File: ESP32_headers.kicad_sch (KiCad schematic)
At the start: 2 parts, among them J1 Conn_01x15_Socket, J2 Conn_01x15_Socket

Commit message: merge labels
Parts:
- removed J1, J2: Conn_01x15_Socket, Connector_PinSocket_2.54mm:PinSocket_1x15_P2.54mm_Vertical, symbol Connector:Conn_01x15_Socket
- added J8, J9: Conn_01x15_Socket, Connector_PinSocket_2.54mm:PinSocket_1x15_P2.54mm_Vertical, symbol Connector:Conn_01x15_Socket
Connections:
- new net +5V: J8.15 (Pin_15)
- new net 3.3V: J9.1 (Pin_1)
- new net D12: J8.12 (Pin_12)
- new net D13: J8.13 (Pin_13)
- new net D14: J8.11 (Pin_11)
- new net D15: J9.3 (Pin_3)
- new net D18: J9.9 (Pin_9)
- new net D19: J9.10 (Pin_10)
- new net D2: J9.4 (Pin_4)
- new net D21: J9.11 (Pin_11)
- new net D22: J9.14 (Pin_14)
- new net D23: J9.15 (Pin_15)
- new net D25: J8.8 (Pin_8)
- new net D26: J8.9 (Pin_9)
- new net D27: J8.10 (Pin_10)
- new net D32: J8.6 (Pin_6)
- new net D33: J8.7 (Pin_7)
- new net D34: J8.4 (Pin_4)
- new net D35: J8.5 (Pin_5)
- new net D4: J9.5 (Pin_5)
- new net D5: J9.8 (Pin_8)
- new net EN: J8.1 (Pin_1)
- new net GND: J8.14 (Pin_14), J9.2 (Pin_2)
- new net RX: J9.12 (Pin_12)
- new net RX2: J9.6 (Pin_6)
- new net TX: J9.13 (Pin_13)
- new net TX2: J9.7 (Pin_7)
- new net VN: J8.3 (Pin_3)
- new net VP: J8.2 (Pin_2)

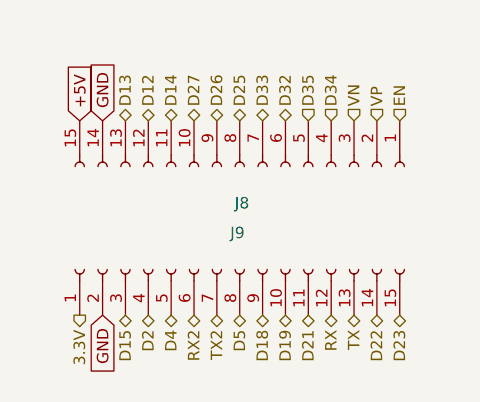
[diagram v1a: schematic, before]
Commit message: PCB Wiring to ESP32
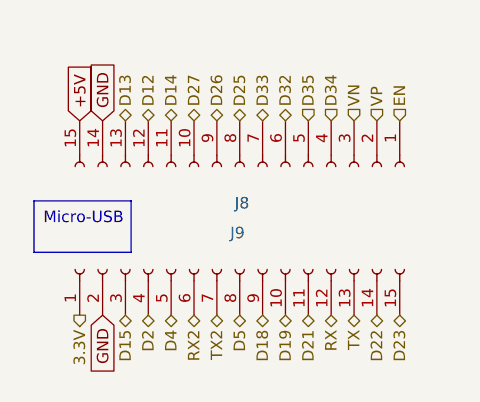
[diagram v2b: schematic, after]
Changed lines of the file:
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@@
 	(generator_version "8.0")
 	(paper "A4")
+	(text_box "Micro-USB"
+		(exclude_from_sim no)
+		(at 35.56 63.5 0)
+		(size 10.795 5.715)
+		(stroke
+			(width 0)
+			(type default)
+		)
+		(fill
+			(type none)
+		)
+		(effects
+			(font
+				(size 1.27 1.27)
+			)
+			(justify left top)
+		)
+	)
 	(global_label "GND"
 		(shape input)

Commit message: mounting holes
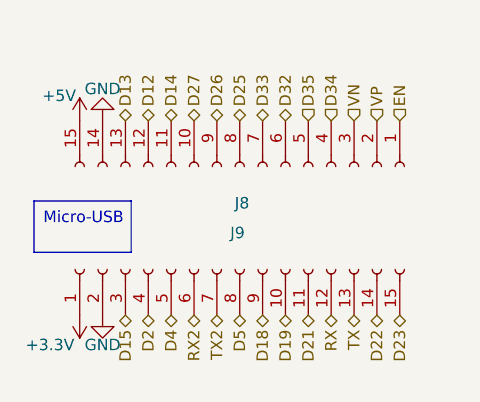
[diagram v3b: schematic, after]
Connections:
- net 3.3V renamed +3.3V

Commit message: adds test & test points
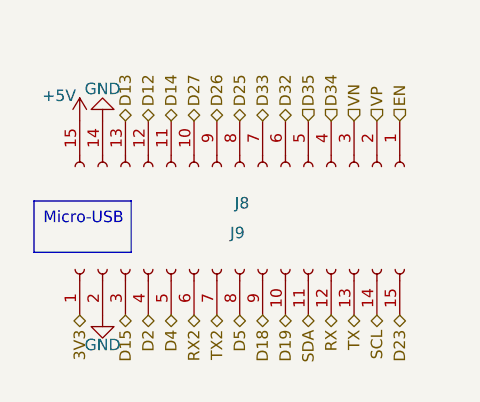
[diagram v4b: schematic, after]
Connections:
- net +3.3V renamed 3V3
- net D21 renamed SDA
- net D22 renamed SCL
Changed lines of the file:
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@@
 		)
 	)
-	(hierarchical_label "D21"
+	(hierarchical_label "SDA"
 		(shape bidirectional)
 		(at 66.04 76.2 270)
@@
 		)
 	)
-	(hierarchical_label "D22"
+	(hierarchical_label "SCL"
 		(shape bidirectional)
 		(at 73.66 76.2 270)
@@
 			)
 			(justify left)
+		)
+	)
+	(hierarchical_label "3V3"
+		(shape bidirectional)
+		(at 40.64 76.2 270)
+		(fields_autoplaced yes)
+		(effects
+			(font
+				(size 1.27 1.27)
+			)
+			(justify right)
 		)
 	)
@@
 					(unit 1)
 				)
-			)
-		)
-	)
-	(symbol
-		(lib_id "power:+3.3V")
-		(at 40.64 76.2 180)
-		(unit 1)
-		(exclude_from_sim no)
-		(in_bom yes)
-		(on_board yes)
-		(dnp no)
-		(property "Reference" "#PWR050"
-			(at 40.64 72.39 0)
-			(effects
-				(font
-					(size 1.27 1.27)
-				)
-				(hide yes)
-			)
-		)
-		(property "Value" "+3.3V"
-			(at 37.338 79.502 0)
-			(effects
-				(font
-					(size 1.27 1.27)
-				)
-			)
-		)
-		(property "Footprint" ""
-			(at 40.64 76.2 0)
-			(effects
-				(font
-					(size 1.27 1.27)
-				)
-				(hide yes)
-			)
-		)
-		(property "Datasheet" ""
-			(at 40.64 76.2 0)
-			(effects
-				(font
-					(size 1.27 1.27)
-				)
-				(hide yes)
-			)
-		)
-		(property "Description" "Power symbol creates a global label with name \"+3.3V\""
-			(at 40.64 76.2 0)
-			(effects
-				(font
-					(size 1.27 1.27)
-				)
-				(hide yes)
-			)
-		)
-		(pin "1"
-		)
-		(instances
-			(project "JAS Warhead PCB"
-				(path "/a037544f-9a20-478c-bac0-d162f9edf245/e02061e8-dea8-4b91-abef-2bf744ccc8cc"
-					(reference "#PWR050")
-					(unit 1)
-				)

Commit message: start compliance with PCBway
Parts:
- J8, J9: Item # (none) -> 11
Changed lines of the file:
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@@
+			)
+		)
+		(property "Item #" "11"
+			(at 58.42 59.69 0)
+			(effects
+				(font
+					(size 1.27 1.27)
+				)
+				(hide yes)
 			)
 		)
@@
 			(at 58.42 71.12 0)
 			(effects
+				(font
+					(size 1.27 1.27)
+				)
+				(hide yes)
+			)
+		)
+		(property "Item #" "11"
+			(at 58.42 71.12 0)
+			(effects

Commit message: refresh stage 1
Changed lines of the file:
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@@
 	(generator_version "8.0")
 	(paper "A4")
+	(wire
+		(pts
+			(xy 40.64 52.07) (xy 40.64 54.61)
+		)
+		(stroke
+			(width 0)
+			(type default)
+		)
+	)
+	(wire
+		(pts
+			(xy 43.18 52.07) (xy 43.18 54.61)
+		)
+		(stroke
+			(width 0)
+			(type default)
+		)
+	)
 	(text_box "Micro-USB"
 		(exclude_from_sim no)
@@
 	(symbol
 		(lib_id "power:GND")
-		(at 43.18 54.61 180)
+		(at 43.18 52.07 180)
 		(unit 1)
 		(exclude_from_sim no)
@@
 		(dnp no)
 		(property "Reference" "#PWR08"
-			(at 43.18 48.26 0)
+			(at 43.18 45.72 0)
 			(effects
 				(font
@@
 		)
 		(property "Value" "GND"
-			(at 43.18 51.054 0)
+			(at 43.18 48.514 0)
 			(effects
 				(font
@@
 		)
 		(property "Footprint" ""
-			(at 43.18 54.61 0)
+			(at 43.18 52.07 0)
 			(effects
 				(font
@@
 		)
 		(property "Datasheet" ""
-			(at 43.18 54.61 0)
+			(at 43.18 52.07 0)
 			(effects
 				(font
@@
 		)
 		(property "Description" "Power symbol creates a global label with name \"GND\" , ground"
-			(at 43.18 54.61 0)
+			(at 43.18 52.07 0)
 			(effects
 				(font
@@
 	(symbol
 		(lib_id "power:+5V")
-		(at 40.64 54.61 0)
+		(at 40.64 52.07 0)
 		(unit 1)
 		(exclude_from_sim no)
@@
 		(dnp no)
 		(property "Reference" "#PWR06"
-			(at 40.64 58.42 0)
+			(at 40.64 55.88 0)
 			(effects
 				(font
@@
 		)
 		(property "Value" "+5V"
-			(at 38.354 51.816 0)
+			(at 38.354 49.276 0)
 			(effects
 				(font
@@
 		)
 		(property "Footprint" ""
-			(at 40.64 54.61 0)
+			(at 40.64 52.07 0)
 			(effects
 				(font
@@
 		)
 		(property "Datasheet" ""
-			(at 40.64 54.61 0)
+			(at 40.64 52.07 0)
 			(effects
 				(font
@@
 		)
 		(property "Description" "Power symbol creates a global label with name \"+5V\""
-			(at 40.64 54.61 0)
-			(effects
-				(font
+			(at 40.64 52.07 0)
+			(effects
+				(font

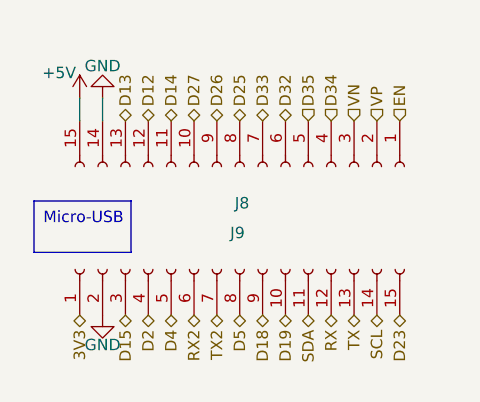
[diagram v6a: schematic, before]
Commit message: progress toward final board, need smaller relays
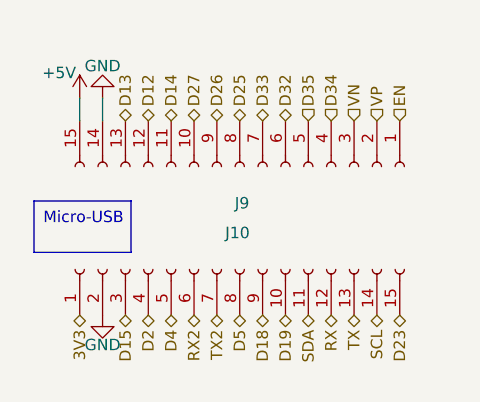
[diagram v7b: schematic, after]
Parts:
- renumbered J9 to J10, J8 to J9
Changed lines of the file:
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@@
 		(on_board yes)
 		(dnp no)
-		(property "Reference" "#PWR07"
+		(property "Reference" "#PWR028"
 			(at 43.18 82.55 0)
 			(effects
@@
 			(project "JAS Warhead PCB"
 				(path "/a037544f-9a20-478c-bac0-d162f9edf245/e02061e8-dea8-4b91-abef-2bf744ccc8cc"
-					(reference "#PWR07")
+					(reference "#PWR028")
 					(unit 1)
 				)
@@
 		(on_board yes)
 		(dnp no)
-		(property "Reference" "#PWR08"
+		(property "Reference" "#PWR027"
 			(at 43.18 45.72 0)
 			(effects
@@
 			(project "JAS Warhead PCB"
 				(path "/a037544f-9a20-478c-bac0-d162f9edf245/e02061e8-dea8-4b91-abef-2bf744ccc8cc"
-					(reference "#PWR08")
+					(reference "#PWR027")
 					(unit 1)
 				)
@@
 		(on_board yes)
 		(dnp no)
-		(property "Reference" "J8"
+		(property "Reference" "J9"
 			(at 58.674 63.754 90)
 			(effects
@@
 			(project "JAS Warhead PCB"
 				(path "/a037544f-9a20-478c-bac0-d162f9edf245/e02061e8-dea8-4b91-abef-2bf744ccc8cc"
-					(reference "J8")
+					(reference "J9")
 					(unit 1)
 				)
@@
 		(on_board yes)
 		(dnp no)
-		(property "Reference" "J9"
+		(property "Reference" "J10"
 			(at 58.166 67.056 90)
 			(effects
@@
 			(project "JAS Warhead PCB"
 				(path "/a037544f-9a20-478c-bac0-d162f9edf245/e02061e8-dea8-4b91-abef-2bf744ccc8cc"
-					(reference "J9")
+					(reference "J10")
 					(unit 1)
 				)
@@
 		(on_board yes)
 		(dnp no)
-		(property "Reference" "#PWR06"
+		(property "Reference" "#PWR026"
 			(at 40.64 55.88 0)
 			(effects
@@
 			(project "JAS Warhead PCB"
 				(path "/a037544f-9a20-478c-bac0-d162f9edf245/e02061e8-dea8-4b91-abef-2bf744ccc8cc"
-					(reference "#PWR06")
-					(unit 1)
-				)
+					(reference "#PWR026")
+					(unit 1)
+				)

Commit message: docs
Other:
- company: (none) -> Jet & Aeronautics Society
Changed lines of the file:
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@@
 	(generator_version "8.0")
 	(paper "A4")
+	(title_block
+		(date "2024-04-21")
+		(company "Jet & Aeronautics Society")
+	)
 	(wire
 		(pts
